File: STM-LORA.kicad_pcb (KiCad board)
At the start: 2 copper layers, 56.5 x 53.3 mm, 55 parts, among them J1 Batt, J10 CONN_02X07, J11 CONN_02X09, J12 CONN_01X02, J13 CONN_01X02, J14 CONN_01X02, J15 CONN_01X03, J16 CONN_01X01, J2 Solar, J3 CONN_01X17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

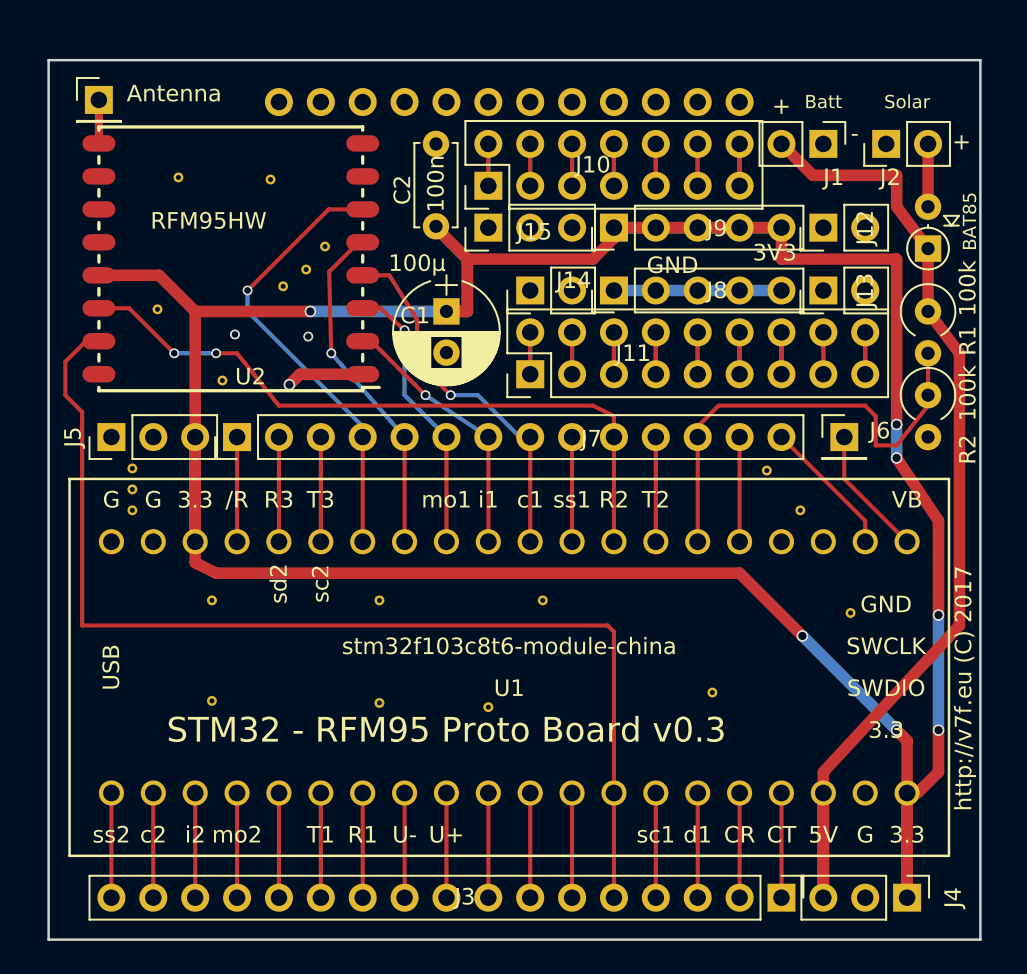
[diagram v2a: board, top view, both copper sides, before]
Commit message: Add 5 mounting holes (2mm)
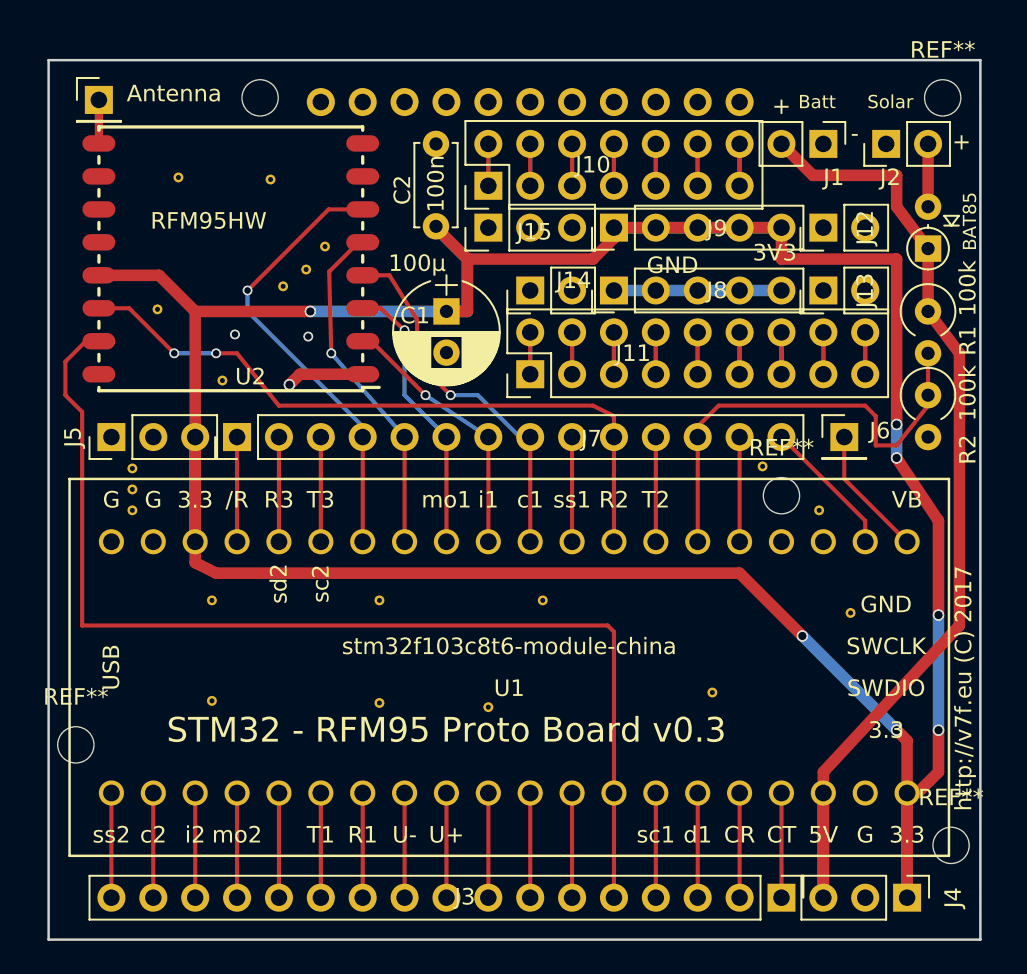
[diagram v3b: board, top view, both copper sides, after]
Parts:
- removed the REF** at (97.8, 55.9)
- added REF**: MountingHole_2.2mm_M2_DIN965, Mounting_Holes:MountingHole_2.2mm_M2_DIN965, F.Cu at (138.6, 101.0)
- added REF**: MountingHole_2.2mm_M2_DIN965, Mounting_Holes:MountingHole_2.2mm_M2_DIN965, F.Cu at (85.5, 94.9)
- added REF**: MountingHole_2.2mm_M2_DIN965, Mounting_Holes:MountingHole_2.2mm_M2_DIN965, F.Cu at (96.6, 55.6)
- added REF**: MountingHole_2.2mm_M2_DIN965, Mounting_Holes:MountingHole_2.2mm_M2_DIN965, F.Cu at (128.3, 79.8)
- added REF**: MountingHole_2.2mm_M2_DIN965, Mounting_Holes:MountingHole_2.2mm_M2_DIN965, F.Cu at (138.0, 55.6)
- moved REF** 1.14 mm to (130.6, 80.6)
- moved REF** 0.36 mm to (127.1, 78.0)
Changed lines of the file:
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@@
     (links 111)
     (no_connects 0)
-    (area 81.834667 52.448 140.648 109.173333)
+    (area 83.744999 53.264999 140.410001 106.755001)
     (thickness 1.6)
     (drawings 12)
     (tracks 199)
     (zones 0)
-    (modules 55)
+    (modules 59)
     (nets 69)
   )
@@
     (add_net VCC)
   )
+  (module Mounting_Holes:MountingHole_2.2mm_M2_DIN965 (layer F.Cu)
+    (at 138.557 100.965)
+    (descr "Mounting Hole 2.2mm, no annular, M2, DIN965")
+    (tags "mounting hole 2.2mm no annular m2 din965")
+    (fp_text reference REF** (at 0 -2.9) (layer F.SilkS)
+      (effects (font (size 1 1) (thickness 0.15)))
+    )
+    (fp_text value MountingHole_2.2mm_M2_DIN965 (at 0 2.9) (layer F.Fab) hide
+      (effects (font (size 1 1) (thickness 0.15)))
+    )
+    (fp_circle (center 0 0) (end 1.9 0) (layer Cmts.User) (width 0.15))
+    (fp_circle (center 0 0) (end 2.15 0) (layer F.CrtYd) (width 0.05))
+    (pad 1 np_thru_hole circle (at 0 0) (size 2.2 2.2) (drill 2.2) (layers *.Cu *.Mask))
+  )
+  (module Mounting_Holes:MountingHole_2.2mm_M2_DIN965 (layer F.Cu)
+    (at 85.471 94.869)
+    (descr "Mounting Hole 2.2mm, no annular, M2, DIN965")
+    (tags "mounting hole 2.2mm no annular m2 din965")
+    (fp_text reference REF** (at 0 -2.9) (layer F.SilkS)
+      (effects (font (size 1 1) (thickness 0.15)))
+    )
+    (fp_text value MountingHole_2.2mm_M2_DIN965 (at 0 2.9) (layer F.Fab) hide
+      (effects (font (size 1 1) (thickness 0.15)))
+    )
+    (fp_circle (center 0 0) (end 1.9 0) (layer Cmts.User) (width 0.15))
+    (fp_circle (center 0 0) (end 2.15 0) (layer F.CrtYd) (width 0.05))
+    (pad 1 np_thru_hole circle (at 0 0) (size 2.2 2.2) (drill 2.2) (layers *.Cu *.Mask))
+  )
+  (module Mounting_Holes:MountingHole_2.2mm_M2_DIN965 (layer F.Cu)
+    (at 96.647 55.626)
+    (descr "Mounting Hole 2.2mm, no annular, M2, DIN965")
+    (tags "mounting hole 2.2mm no annular m2 din965")
+    (fp_text reference REF** (at 0 -2.9) (layer F.SilkS) hide
+      (effects (font (size 1 1) (thickness 0.15)))
+    )
+    (fp_text value MountingHole_2.2mm_M2_DIN965 (at 0 2.9) (layer F.Fab)
+      (effects (font (size 1 1) (thickness 0.15)))
+    )
+    (fp_circle (center 0 0) (end 1.9 0) (layer Cmts.User) (width 0.15))
+    (fp_circle (center 0 0) (end 2.15 0) (layer F.CrtYd) (width 0.05))
+    (pad 1 np_thru_hole circle (at 0 0) (size 2.2 2.2) (drill 2.2) (layers *.Cu *.Mask))
+  )
+  (module Mounting_Holes:MountingHole_2.2mm_M2_DIN965 (layer F.Cu)
+    (at 138.049 55.626)
+    (descr "Mounting Hole 2.2mm, no annular, M2, DIN965")
+    (tags "mounting hole 2.2mm no annular m2 din965")
+    (fp_text reference REF** (at 0 -2.9) (layer F.SilkS)
+      (effects (font (size 1 1) (thickness 0.15)))
+    )
+    (fp_text value MountingHole_2.2mm_M2_DIN965 (at 0 2.9) (layer F.Fab) hide
+      (effects (font (size 1 1) (thickness 0.15)))
+    )
+    (fp_circle (center 0 0) (end 1.9 0) (layer Cmts.User) (width 0.15))
+    (fp_circle (center 0 0) (end 2.15 0) (layer F.CrtYd) (width 0.05))
+    (pad 1 np_thru_hole circle (at 0 0) (size 2.2 2.2) (drill 2.2) (layers *.Cu *.Mask))
+  )
   (module VIA-0.6mm (layer F.Cu)
     (at 88.9 78.105)
@@
   )
   (module Exp-Area-Pad (layer F.Cu)
-    (at 97.79 55.88)
-    (fp_text reference REF** (at 0 0.5) (layer F.SilkS) hide
-      (effects (font (size 0.127 0.127) (thickness 0.015)))
-    )
-    (fp_text value Exp-Area-Pad (at 0 -0.5) (layer F.Fab) hide
-      (effects (font (size 0.127 0.127) (thickness 0.015)))
-    )
-    (pad 1 thru_hole circle (at 0 0) (size 1.7 1.7) (drill 1) (layers *.Cu *.Mask))
-  )
-  (module Exp-Area-Pad (layer F.Cu)
     (at 100.33 55.88)
     (fp_text reference REF** (at 0 0.5) (layer F.SilkS) hide
@@
   )
   (module VIA-0.6mm (layer F.Cu)
-    (at 129.413 80.645)
+    (at 130.556 80.645)
     (fp_text reference REF** (at 0 0.5) (layer F.SilkS) hide
       (effects (font (size 0.127 0.127) (thickness 0.015)))
@@
   )
   (module VIA-0.6mm (layer F.Cu)
-    (at 127.381 78.232)
+    (at 127.127 77.978)
     (fp_text reference REF** (at 0 0.5) (layer F.SilkS) hide
       (effects (font (size 0.127 0.127) (thickness 0.015)))
@@
       (effects (font (size 1 1) (thickness 0.15)))
     )
-    (fp_text value Batt (at -2.54 0 360) (layer F.SilkS)
+    (fp_text value Batt (at -2.54 0.381 360) (layer F.SilkS)
       (effects (font (size 0.8 0.8) (thickness 0.15)))
     )
@@
       (effects (font (size 1 1) (thickness 0.15)))
     )
-    (fp_text value Solar (at 2.54 1.27 180) (layer F.SilkS)
+    (fp_text value Solar (at 2.54 0.254 180) (layer F.SilkS)
       (effects (font (size 0.8 0.8) (thickness 0.15)))
     )
@@
     )
   )
+  (module Mounting_Holes:MountingHole_2.2mm_M2_DIN965 (layer F.Cu)
+    (at 128.27 79.756)
+    (descr "Mounting Hole 2.2mm, no annular, M2, DIN965")
+    (tags "mounting hole 2.2mm no annular m2 din965")
+    (fp_text reference REF** (at 0 -2.9) (layer F.SilkS)
+      (effects (font (size 1 1) (thickness 0.15)))
+    )
+    (fp_text value MountingHole_2.2mm_M2_DIN965 (at 0 2.9) (layer F.Fab) hide
+      (effects (font (size 1 1) (thickness 0.15)))
+    )
+    (fp_circle (center 0 0) (end 1.9 0) (layer Cmts.User) (width 0.15))
+    (fp_circle (center 0 0) (end 2.15 0) (layer F.CrtYd) (width 0.05))
+    (pad 1 np_thru_hole circle (at 0 0) (size 2.2 2.2) (drill 2.2) (layers *.Cu *.Mask))
+  )
   (gr_text + (at 139.192 58.293) (layer F.SilkS)

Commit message: Move 3 holes to corner
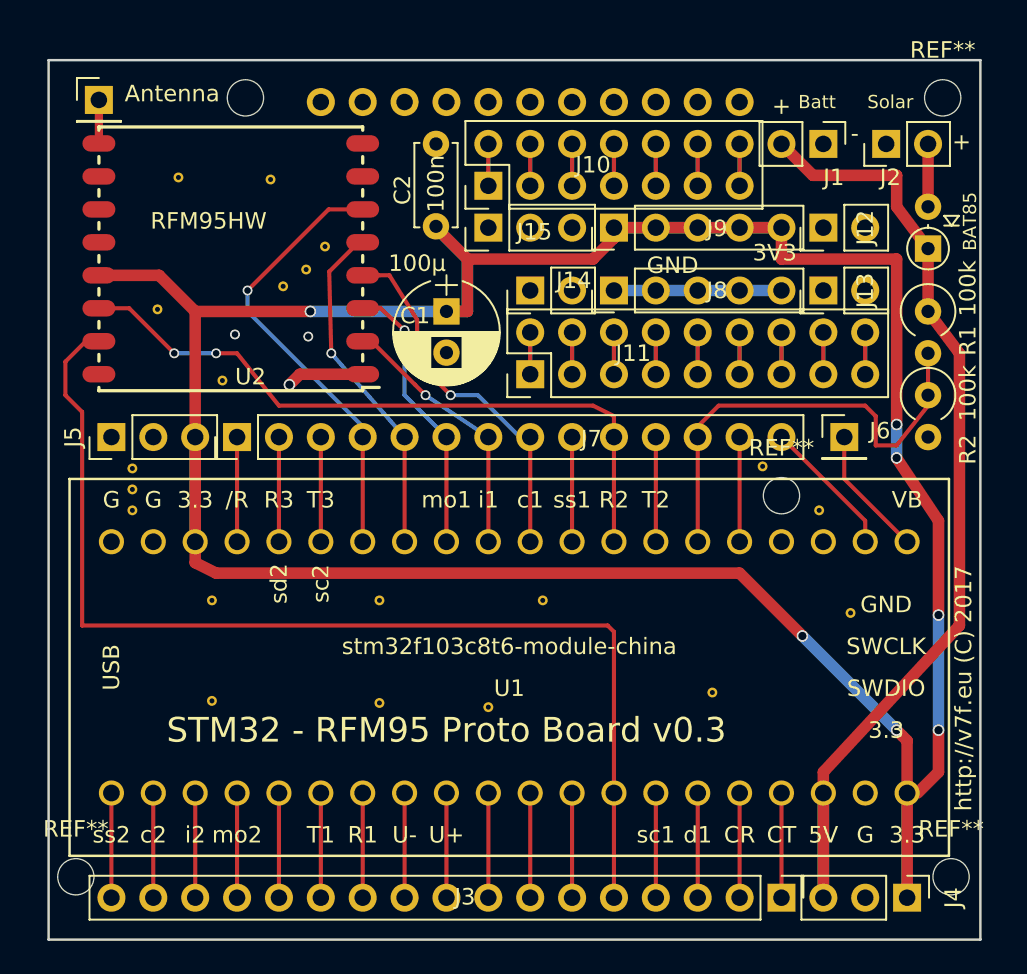
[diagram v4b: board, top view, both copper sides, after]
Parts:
- moved REF** 8.00 mm to (85.5, 102.9)
- moved REF** 1.91 mm to (138.6, 102.9)
- moved REF** 0.89 mm to (95.8, 55.6)
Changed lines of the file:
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@@
   )
   (module Mounting_Holes:MountingHole_2.2mm_M2_DIN965 (layer F.Cu)
-    (at 138.557 100.965)
+    (at 138.557 102.87)
     (descr "Mounting Hole 2.2mm, no annular, M2, DIN965")
     (tags "mounting hole 2.2mm no annular m2 din965")
@@
   )
   (module Mounting_Holes:MountingHole_2.2mm_M2_DIN965 (layer F.Cu)
-    (at 85.471 94.869)
+    (at 85.471 102.87)
     (descr "Mounting Hole 2.2mm, no annular, M2, DIN965")
     (tags "mounting hole 2.2mm no annular m2 din965")
@@
   )
   (module Mounting_Holes:MountingHole_2.2mm_M2_DIN965 (layer F.Cu)
-    (at 96.647 55.626)
+    (at 95.758 55.626)
     (descr "Mounting Hole 2.2mm, no annular, M2, DIN965")
     (tags "mounting hole 2.2mm no annular m2 din965")
@@
     (effects (font (size 1 1) (thickness 0.25)))
   )
-  (gr_text Antenna (at 91.44 55.372) (layer F.SilkS)
+  (gr_text Antenna (at 91.313 55.372) (layer F.SilkS)
     (effects (font (size 1 1) (thickness 0.15)))
   )

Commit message: bigger antenna hole (1.3mm) and moved mounting holes
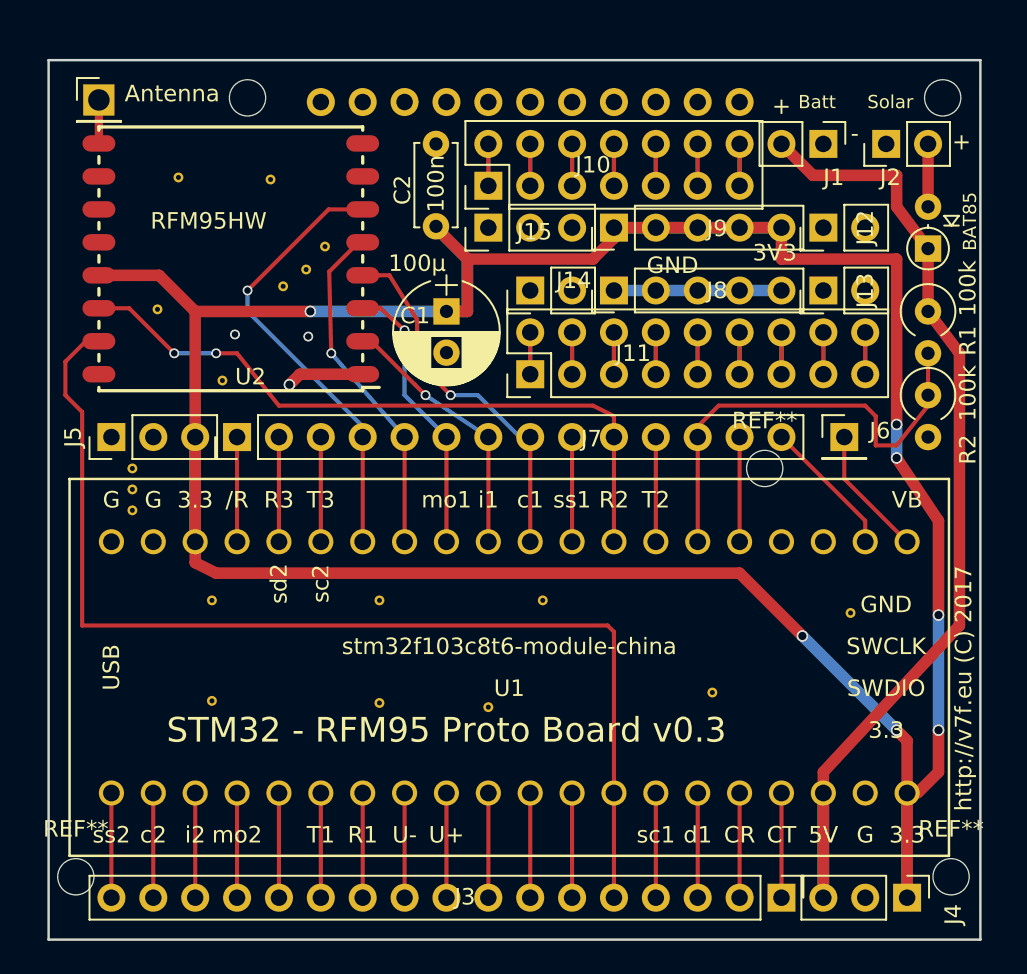
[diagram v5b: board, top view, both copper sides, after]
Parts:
- removed the REF** at (130.6, 80.6)
- removed the REF** at (127.1, 78.0)
- REF** (x2): value MountingHole_2.2mm_M2_DIN965 -> (none)
- moved REF** 1.94 mm to (127.3, 78.1)
- moved ? 0.13 mm to (95.9, 55.6)
- renumbered REF** to ?
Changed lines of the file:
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@@
     (tracks 199)
     (zones 0)
-    (modules 59)
+    (modules 57)
     (nets 69)
   )
@@
     (mod_text_size 1 1)
     (mod_text_width 0.15)
-    (pad_size 1.7 1.7)
-    (pad_drill 1)
+    (pad_size 1.9 1.9)
+    (pad_drill 1.3)
     (pad_to_mask_clearance 0.2)
     (aux_axis_origin 0 0)
@@
       (effects (font (size 1 1) (thickness 0.15)))
     )
-    (fp_text value MountingHole_2.2mm_M2_DIN965 (at 0 2.9) (layer F.Fab) hide
+    (fp_text value "" (at 0 2.9) (layer F.Fab) hide
       (effects (font (size 1 1) (thickness 0.15)))
     )
@@
       (effects (font (size 1 1) (thickness 0.15)))
     )
-    (fp_text value MountingHole_2.2mm_M2_DIN965 (at 0 2.9) (layer F.Fab) hide
+    (fp_text value "" (at 0 2.9) (layer F.Fab) hide
       (effects (font (size 1 1) (thickness 0.15)))
     )
@@
   )
   (module Mounting_Holes:MountingHole_2.2mm_M2_DIN965 (layer F.Cu)
-    (at 95.758 55.626)
+    (at 95.885 55.626)
     (descr "Mounting Hole 2.2mm, no annular, M2, DIN965")
     (tags "mounting hole 2.2mm no annular m2 din965")
-    (fp_text reference REF** (at 0 -2.9) (layer F.SilkS) hide
+    (fp_text reference "" (at 0 -2.9) (layer F.SilkS) hide
       (effects (font (size 1 1) (thickness 0.15)))
     )
@@
     (descr "Mounting Hole 2.2mm, no annular, M2, DIN965")
     (tags "mounting hole 2.2mm no annular m2 din965")
-    (fp_text reference REF** (at 0 -2.9) (layer F.SilkS)
+    (fp_text reference "" (at 0 -2.9) (layer F.SilkS) hide
       (effects (font (size 1 1) (thickness 0.15)))
     )
@@
   (module VIA-0.6mm (layer F.Cu)
     (at 103.886 86.106)
-    (fp_text reference REF** (at 0 0.5) (layer F.SilkS) hide
-      (effects (font (size 0.127 0.127) (thickness 0.015)))
-    )
-    (fp_text value VIA-0.6mm (at 0 -0.5) (layer F.Fab) hide
-      (effects (font (size 0.127 0.127) (thickness 0.015)))
-    )
-    (pad 1 thru_hole circle (at 0 0) (size 0.6 0.6) (drill 0.3) (layers *.Cu)
-      (net 7 GND) (zone_connect 2))
-  )
-  (module VIA-0.6mm (layer F.Cu)
-    (at 130.556 80.645)
-    (fp_text reference REF** (at 0 0.5) (layer F.SilkS) hide
-      (effects (font (size 0.127 0.127) (thickness 0.015)))
-    )
-    (fp_text value VIA-0.6mm (at 0 -0.5) (layer F.Fab) hide
-      (effects (font (size 0.127 0.127) (thickness 0.015)))
-    )
-    (pad 1 thru_hole circle (at 0 0) (size 0.6 0.6) (drill 0.3) (layers *.Cu)
-      (net 7 GND) (zone_connect 2))
-  )
-  (module VIA-0.6mm (layer F.Cu)
-    (at 127.127 77.978)
     (fp_text reference REF** (at 0 0.5) (layer F.SilkS) hide
       (effects (font (size 0.127 0.127) (thickness 0.015)))
@@
     (descr "Through hole straight pin header, 1x03, 2.54mm pitch, single row")
     (tags "Through hole pin header THT 1x03 2.54mm single row")
-    (fp_text reference J4 (at 0 -2.794 270) (layer F.SilkS)
+    (fp_text reference J4 (at 1.016 -2.794 270) (layer F.SilkS)
       (effects (font (size 1 1) (thickness 0.15)))
     )
@@
     (fp_line (start 1.8 6.85) (end 1.8 -1.8) (layer F.CrtYd) (width 0.05))
     (fp_line (start 1.8 -1.8) (end -1.8 -1.8) (layer F.CrtYd) (width 0.05))
-    (fp_text user %R (at 0 -2.33 270) (layer F.Fab)
+    (fp_text user %R (at 1.651 -2.54 270) (layer F.Fab) hide
       (effects (font (size 1 1) (thickness 0.15)))
     )
@@
       (effects (font (size 1 1) (thickness 0.15)))
     )
-    (pad 1 thru_hole rect (at 0 0) (size 1.7 1.7) (drill 1) (layers *.Cu *.Mask)
+    (pad 1 thru_hole rect (at 0 0) (size 1.9 1.9) (drill 1.3) (layers *.Cu *.Mask)
       (net 68 "Net-(J16-Pad1)"))
     (model ${KISYS3DMOD}/Pin_Headers.3dshapes/Pin_Header_Straight_1x01_Pitch2.54mm.wrl
@@
   )
   (module Mounting_Holes:MountingHole_2.2mm_M2_DIN965 (layer F.Cu)
-    (at 128.27 79.756)
+    (at 127.254 78.105)
     (descr "Mounting Hole 2.2mm, no annular, M2, DIN965")
     (tags "mounting hole 2.2mm no annular m2 din965")
